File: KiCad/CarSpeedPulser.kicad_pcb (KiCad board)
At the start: 2 copper layers, 43.2 x 66 mm, 15 parts, among them P1 CONN_01X02, Q1 2SK4017, SW1 RESET, SW2 UP, SW3 DOWN, U1 LPC810, U2 AE-AQM0802, U3 TA48M033F

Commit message: Added writer connector.
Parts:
- added P2: CONN_01X05, Pin_Headers:Pin_Header_Straight_1x05, F.Cu at (58.4, 58.4)
- moved Q1 5.08 mm to (48.3, 66.0)
- moved R2 2.54 mm to (48.3, 58.4)
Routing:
- net Net-(P2-Pad4): track 33.6 -> 66.8 mm, vias 0 -> 1
- net Net-(P2-Pad3): track 41.7 -> 64.1 mm
- net Net-(P2-Pad1): track 41.4 -> 58.8 mm
- net Net-(P2-Pad2): track 15.9 -> 33.2 mm, vias 0 -> 2
- net GND: track 181.9 -> 167.3 mm
- net /PULSE: track 30.0 -> 25.0 mm
- net Net-(SW2-Pad1): track 39.8 -> 36.2 mm
- net Net-(Q1-Pad1): track 16.9 -> 14.8 mm

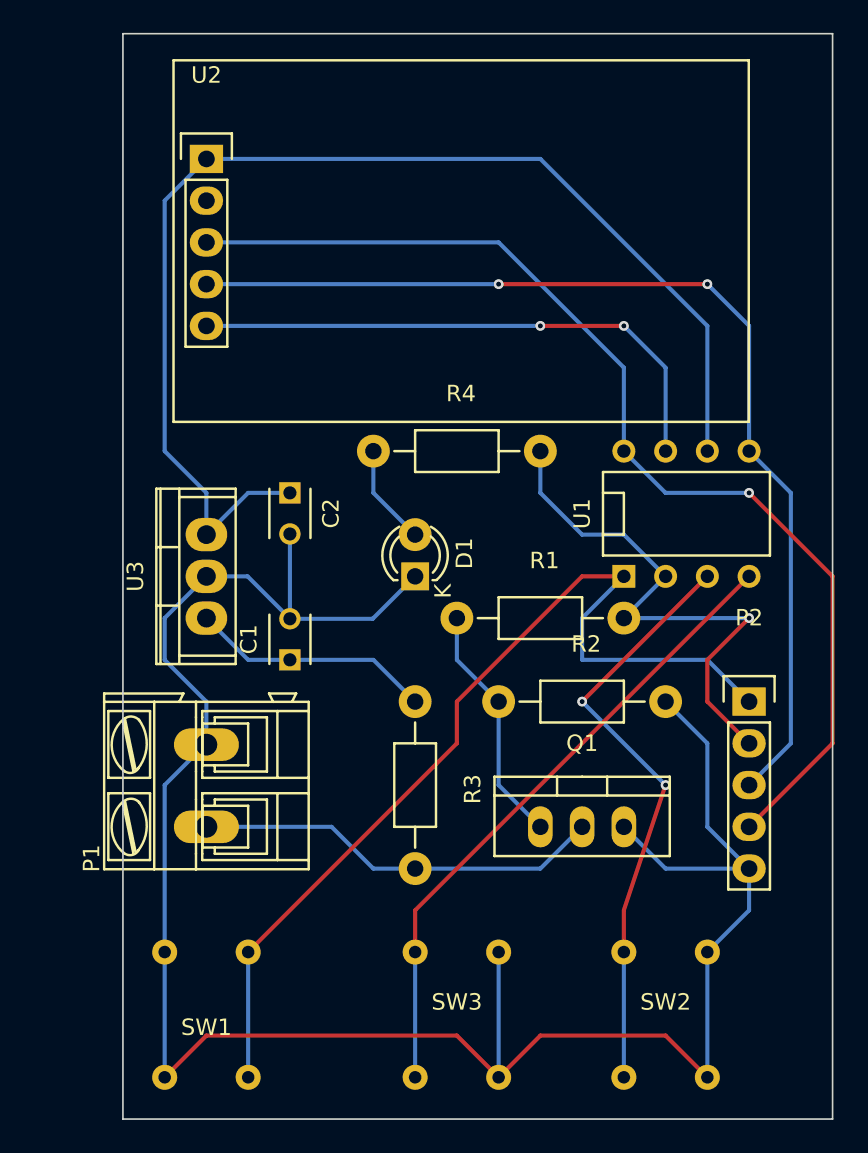
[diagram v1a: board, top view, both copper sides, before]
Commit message: Updated circuit diagram.
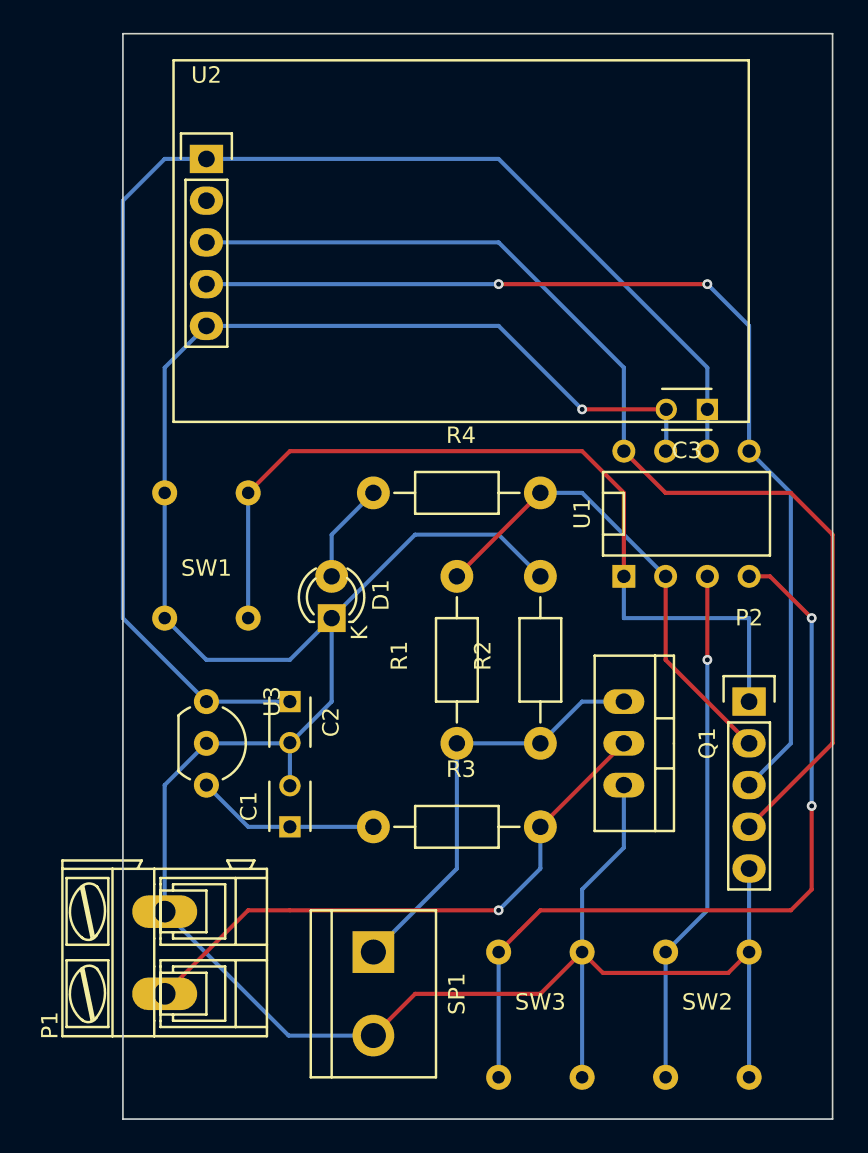
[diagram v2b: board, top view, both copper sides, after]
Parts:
- added C3: 0.1u, Capacitors_ThroughHole:C_Disc_D3_P2.5, F.Cu at (55.9, 40.6)
- added SP1: PiezoSpk, Connect:bornier2, F.Cu at (35.6, 76.2)
- U3: value TA48M033F -> XC6202P332TB; footprint Power_Integrations:TO-220 -> Housings_TO-92:TO-92_Inline_Wide
- moved SW1 27.9 mm to (27.9, 45.7)
- moved C2 12.7 mm to (30.5, 58.4)
- moved P1 10.5 mm to (22.9, 76.2)
- moved C1 10.2 mm to (30.5, 66.0)
- moved U3 7.62 mm to (25.4, 58.4), turned to 270 degrees
- moved Q1 5.68 mm to (50.8, 61.0), turned to 270 degrees
- moved D1 5.68 mm to (33.0, 53.3)
- moved R1 5.68 mm to (40.6, 55.9), turned to 90 degrees
- moved SW3 5.08 mm to (43.2, 81.3)
- moved R3 3.59 mm to (40.6, 66.0), turned to 0 degrees
- moved R2 3.59 mm to (45.7, 55.9), turned to 90 degrees
- moved SW2 2.54 mm to (53.3, 81.3)
- moved R4 2.54 mm to (40.6, 45.7)
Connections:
- U3 pad 1: +12V -> VDD
- U3 pad 3: VDD -> +12V
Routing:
- net GND: track 167.3 -> 180.6 mm, vias 2 -> 1
- net VDD: track 73.4 -> 84.6 mm
- net Net-(Q1-Pad1): track 14.8 -> 26.0 mm
- net /PULSE: track 25.0 -> 35.7 mm, vias 0 -> 1
- net Net-(SW3-Pad1): track 38.9 -> 49.6 mm, vias 0 -> 2
- net Net-(P2-Pad1): track 58.8 -> 52.9 mm
- net Net-(SW2-Pad1): track 36.2 -> 31.5 mm
- net Net-(P2-Pad2): track 33.2 -> 29.2 mm, vias 2 -> 0
- net +12V: track 14.8 -> 11.2 mm
- net Net-(P2-Pad4): track 66.8 -> 68.3 mm, vias 1 -> 0

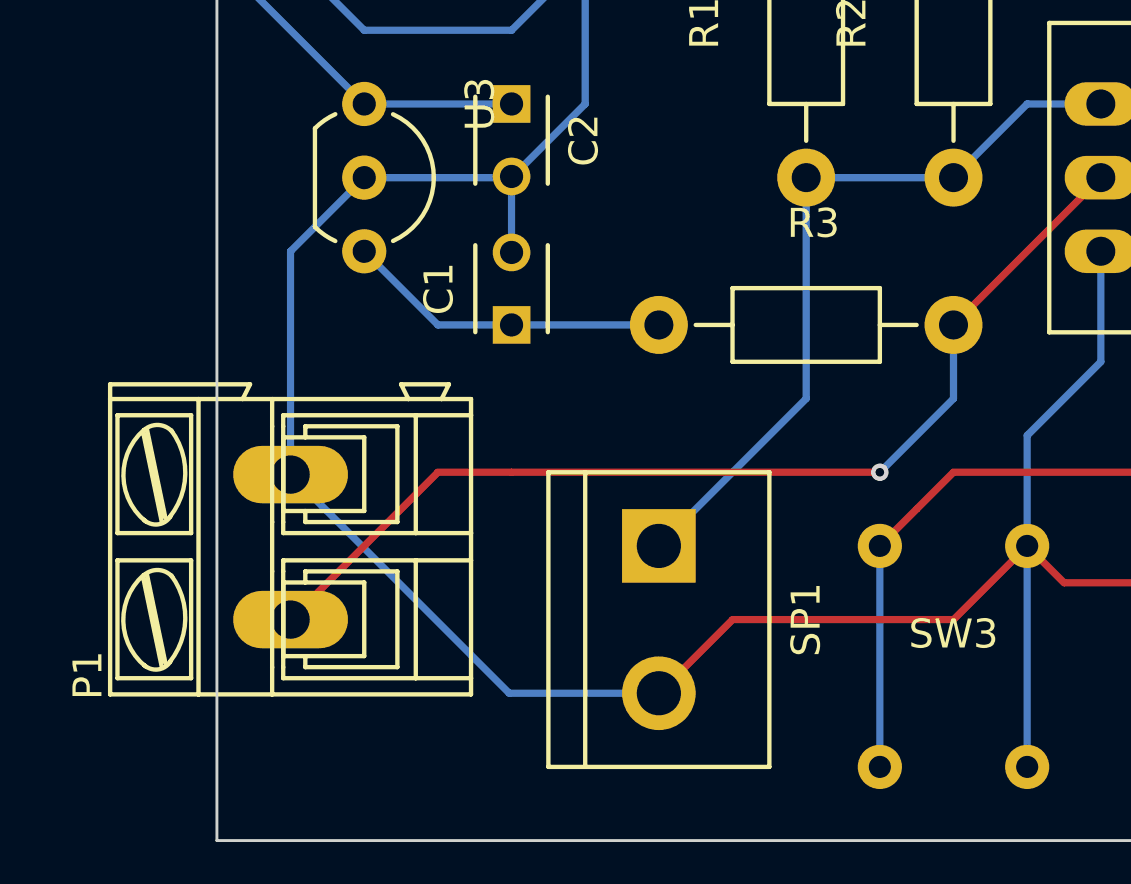
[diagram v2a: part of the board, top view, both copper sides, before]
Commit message: Replaced a connector.
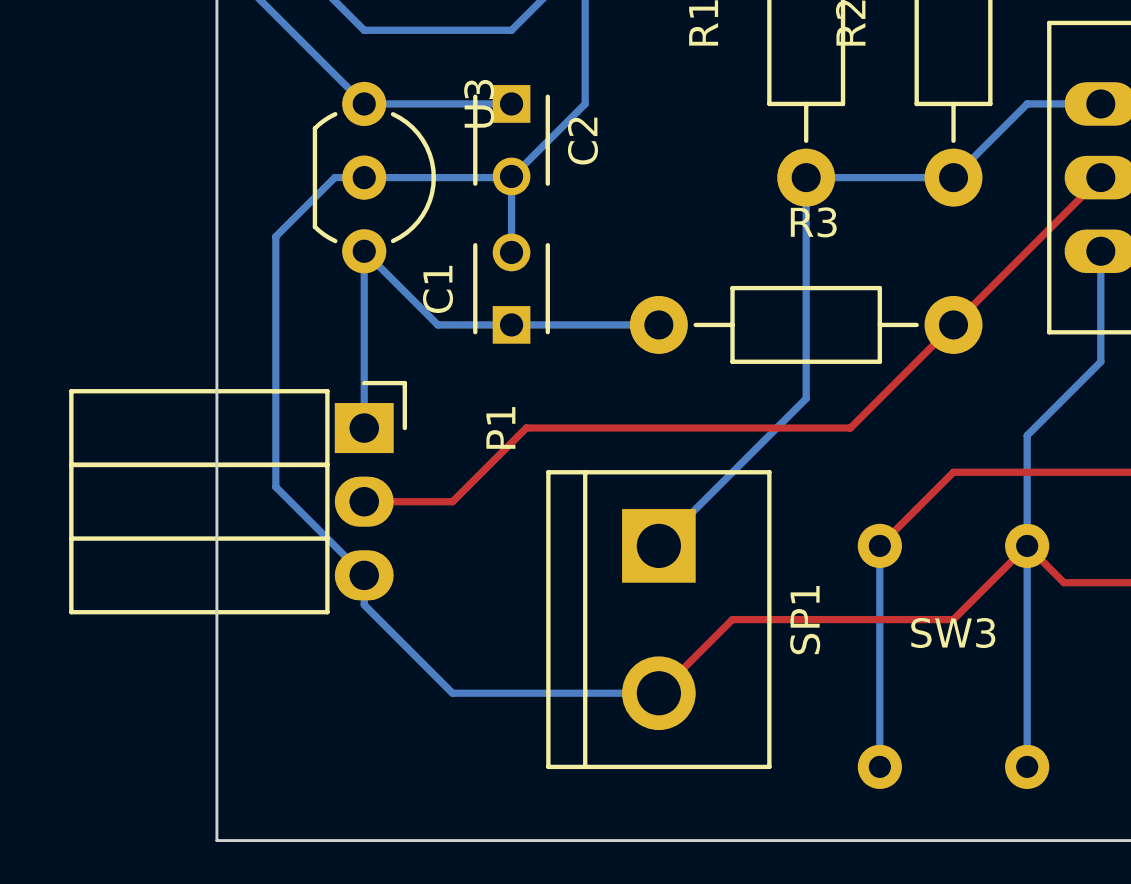
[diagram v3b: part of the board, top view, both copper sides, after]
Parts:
- P1: value CONN_01X02 -> CONN_01X03; footprint Connect:AK300-2 -> Socket_Strips:Socket_Strip_Angled_1x03
- moved P1 7.08 mm to (25.4, 69.6), turned to 270 degrees
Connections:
- P1 pad 1: /PULSE -> +12V
- P1 pad 2: GND -> /PULSE
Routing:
- net +12V: track 11.2 -> 17.3 mm
- net /PULSE: track 35.7 -> 30.0 mm, vias 1 -> 0
- net GND: track 180.6 -> 182.8 mm

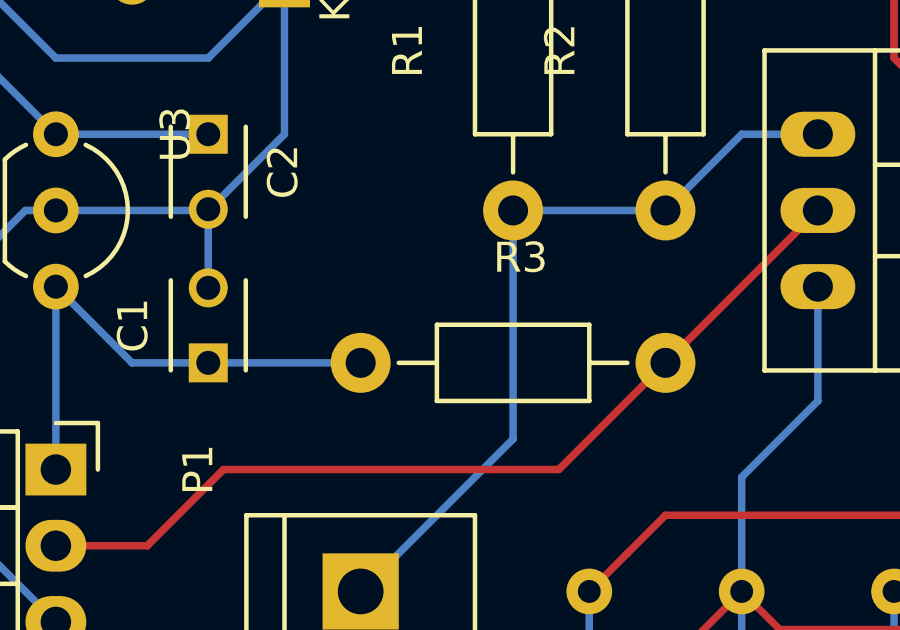
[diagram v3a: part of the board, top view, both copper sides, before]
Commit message: Removed pullup register. PULSE output is open drain.
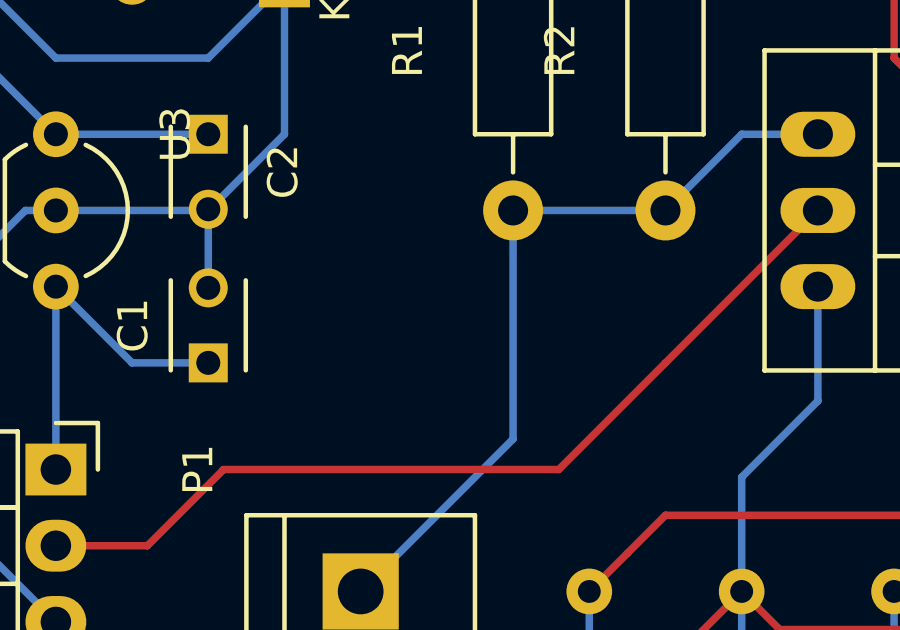
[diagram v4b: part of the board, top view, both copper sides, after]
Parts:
- removed R3: 10k, Resistors_ThroughHole:Resistor_Horizontal_RM10mm
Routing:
- net +12V: track 17.3 -> 12.2 mm
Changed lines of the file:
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@@
-(kicad_pcb (version 4) (host pcbnew "(after 2015-mar-04 BZR unknown)-product")
+(kicad_pcb (version 4) (host pcbnew 4.0.0-rc1-stable)
   (general
-    (links 44)
+    (links 42)
     (no_connects 0)
-    (area 20.269999 17.729999 63.550001 83.870001)
+    (area 14.574999 17.729999 63.825002 83.870001)
     (thickness 1.6)
     (drawings 4)
-    (tracks 112)
+    (tracks 111)
     (zones 0)
-    (modules 18)
+    (modules 17)
     (nets 14)
   )
@@
     )
   )
-  (module Resistors_ThroughHole:Resistor_Horizontal_RM10mm (layer F.Cu)
-    (at 40.64 66.04)
-    (descr "Resistor, Axial,  RM 10mm, 1/3W,")
-    (tags "Resistor, Axial, RM 10mm, 1/3W,")
-    (fp_text reference R3 (at 0.24892 -3.50012) (layer F.SilkS)
-      (effects (font (size 1 1) (thickness 0.15)))
-    )
-    (fp_text value 10k (at 0 0) (layer F.Fab)
-      (effects (font (size 1 1) (thickness 0.15)))
-    )
-    (fp_line (start -2.54 -1.27) (end 2.54 -1.27) (layer F.SilkS) (width 0.15))
-    (fp_line (start 2.54 -1.27) (end 2.54 1.27) (layer F.SilkS) (width 0.15))
-    (fp_line (start 2.54 1.27) (end -2.54 1.27) (layer F.SilkS) (width 0.15))
-    (fp_line (start -2.54 1.27) (end -2.54 -1.27) (layer F.SilkS) (width 0.15))
-    (fp_line (start -2.54 0) (end -3.81 0) (layer F.SilkS) (width 0.15))
-    (fp_line (start 2.54 0) (end 3.81 0) (layer F.SilkS) (width 0.15))
-    (pad 1 thru_hole circle (at -5.08 0) (size 1.99898 1.99898) (drill 1.00076) (layers *.Cu *.SilkS *.Mask)
-      (net 1 +12V))
-    (pad 2 thru_hole circle (at 5.08 0) (size 1.99898 1.99898) (drill 1.00076) (layers *.Cu *.SilkS *.Mask)
-      (net 9 /PULSE))
-    (model Resistors_ThroughHole.3dshapes/Resistor_Horizontal_RM10mm.wrl
-      (at (xyz 0 0 0))
-      (scale (xyz 0.4 0.4 0.4))
-      (rotate (xyz 0 0 0))
-    )
-  )
   (module Sockets_DIP:DIP-8__300 (layer F.Cu)
     (at 54.61 46.99)
@@
   (gr_line (start 63.5 83.82) (end 20.32 83.82) (angle 90) (layer Edge.Cuts) (width 0.1))
   (gr_line (start 63.5 17.78) (end 63.5 83.82) (angle 90) (layer Edge.Cuts) (width 0.1))
-  (segment (start 25.4 63.5) (end 25.4 69.596) (width 0.25) (layer B.Cu) (net 1) (status C00000))
-  (segment (start 30.48 66.04) (end 35.56 66.04) (width 0.25) (layer B.Cu) (net 1))
+  (segment (start 25.4 63.5) (end 25.4 69.596) (width 0.25) (layer B.Cu) (net 1))
   (segment (start 27.94 66.04) (end 30.48 66.04) (width 0.25) (layer B.Cu) (net 1))
   (segment (start 25.4 63.5) (end 27.94 66.04) (width 0.25) (layer B.Cu) (net 1))
-  (segment (start 25.4 60.96) (end 24.384 60.96) (width 0.25) (layer B.Cu) (net 2) (status 400000))
-  (segment (start 22.352 71.628) (end 25.4 74.676) (width 0.25) (layer B.Cu) (net 2) (status 800000))
+  (segment (start 25.4 60.96) (end 24.384 60.96) (width 0.25) (layer B.Cu) (net 2))
+  (segment (start 22.352 71.628) (end 25.4 74.676) (width 0.25) (layer B.Cu) (net 2))
   (segment (start 22.352 62.992) (end 22.352 71.628) (width 0.25) (layer B.Cu) (net 2))
   (segment (start 24.384 60.96) (end 22.352 62.992) (width 0.25) (layer B.Cu) (net 2))
-  (segment (start 25.4 74.676) (end 25.4 75.692) (width 0.25) (layer B.Cu) (net 2) (status 400000))
+  (segment (start 25.4 74.676) (end 25.4 75.692) (width 0.25) (layer B.Cu) (net 2))
   (segment (start 25.4 75.692) (end 28.448 78.74) (width 0.25) (layer B.Cu) (net 2))
-  (segment (start 28.448 78.74) (end 35.56 78.74) (width 0.25) (layer B.Cu) (net 2) (status 800000))
+  (segment (start 28.448 78.74) (end 35.56 78.74) (width 0.25) (layer B.Cu) (net 2))
   (segment (start 22.86 45.72) (end 22.86 53.34) (width 0.25) (layer B.Cu) (net 2))
   (segment (start 22.86 38.1) (end 22.86 45.72) (width 0.25) (layer B.Cu) (net 2))
@@
   (segment (start 33.02 48.26) (end 35.56 45.72) (width 0.25) (layer B.Cu) (net 8))
   (segment (start 33.02 50.8) (end 33.02 48.26) (width 0.25) (layer B.Cu) (net 8))
-  (segment (start 25.4 72.136) (end 28.448 72.136) (width 0.25) (layer F.Cu) (net 9) (status 400000))
-  (segment (start 42.164 69.596) (end 45.72 66.04) (width 0.25) (layer F.Cu) (net 9) (status 800000))
+  (segment (start 25.4 72.136) (end 28.448 72.136) (width 0.25) (layer F.Cu) (net 9))
+  (segment (start 42.164 69.596) (end 45.72 66.04) (width 0.25) (layer F.Cu) (net 9))
   (segment (start 30.988 69.596) (end 42.164 69.596) (width 0.25) (layer F.Cu) (net 9))
   (segment (start 28.448 72.136) (end 30.988 69.596) (width 0.25) (layer F.Cu) (net 9))
